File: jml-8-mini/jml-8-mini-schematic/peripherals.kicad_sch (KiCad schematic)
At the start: 10 parts, among them J2 Conn_01x09_Pin, J3 Conn_01x04_Pin, U4 Z80 CTC, U5 Z80 SIO

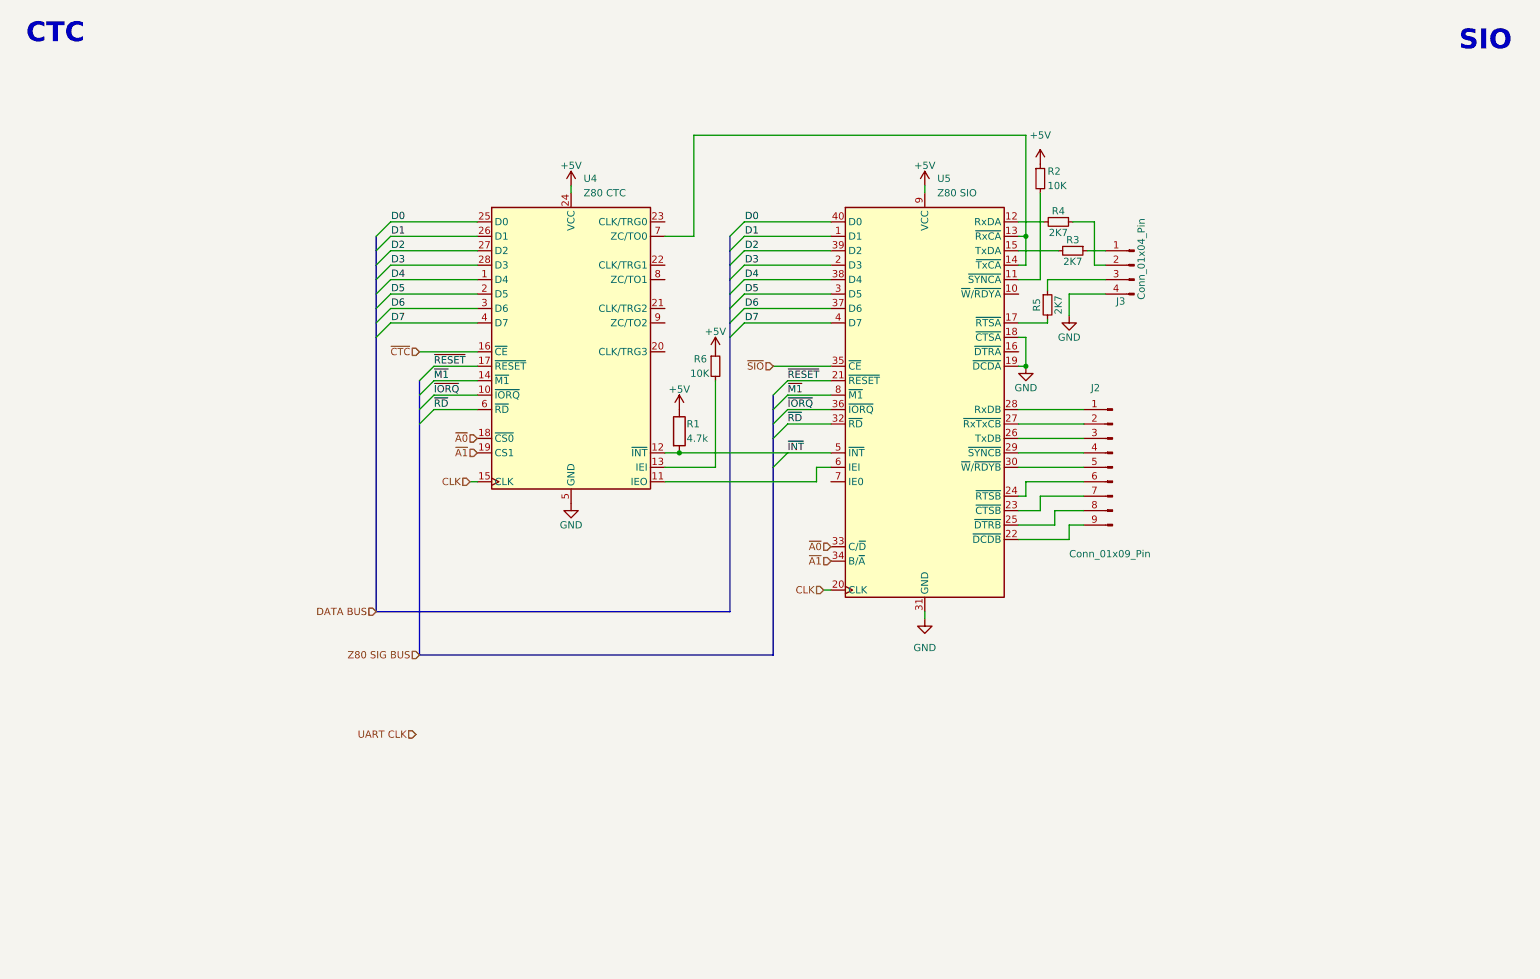
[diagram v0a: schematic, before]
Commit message: lots of changes to schematic, redone to make easier to read and add to
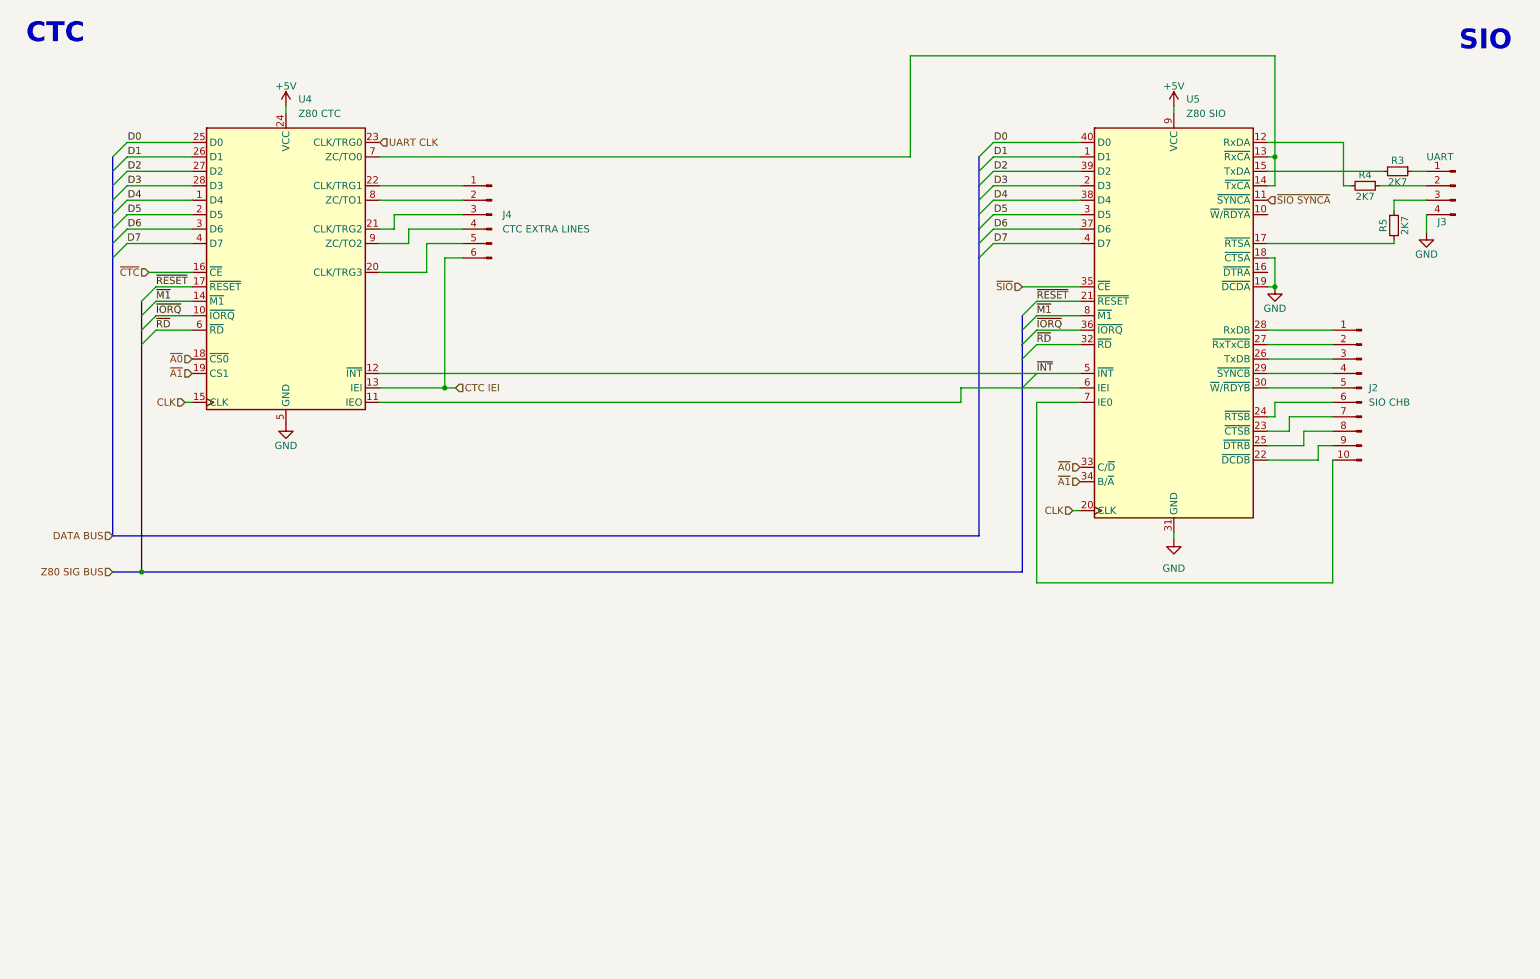
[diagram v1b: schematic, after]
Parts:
- removed J2: Conn_01x09_Pin, symbol Connector:Conn_01x09_Pin
- removed R1: 4.7k, symbol Device:R
- removed R2, R6: 10K, symbol Device:R_Small
- added J2: SIO CHB, symbol Connector:Conn_01x10_Pin
- added J4: CTC EXTRA LINES, symbol Connector:Conn_01x06_Pin
- J3: value Conn_01x04_Pin -> UART
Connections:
- net UART CLK: now also U4.23 (CLK/TRG0)
- net at U5.28 (RxDB): now also J2.1 (Pin_1)
- net at U5.27 (~{RxTxCB}): now also J2.2 (Pin_2)
- net at U5.26 (TxDB): now also J2.3 (Pin_3)
- net at U5.29 (~{SYNCB}): now also J2.4 (Pin_4)
- net at U5.30 (~{W}/~{RDYB}): now also J2.5 (Pin_5)
- net at U5.24 (~{RTSB}): now also J2.6 (Pin_6)
- net at U5.23 (~{CTSB}): now also J2.7 (Pin_7)
- net at U5.25 (~{DTRB}): now also J2.8 (Pin_8)
- net at U5.22 (~{DCDB}): now also J2.9 (Pin_9)
- net CTC IEI: now reaches U4.13 (IEI)
- net CTC IEI: now also J4.6 (Pin_6)
- net ~{SIO SYNCA}: now reaches U5.11 (~{SYNCA})
- net at U5.7 (IE0): now also J2.10 (Pin_10)
- net at U4.20 (CLK/TRG3): now also J4.5 (Pin_5)
- net at U4.21 (CLK/TRG2): now also J4.3 (Pin_3)
- net at U4.22 (CLK/TRG1): now also J4.1 (Pin_1)
- net at U4.8 (ZC/TO1): now also J4.2 (Pin_2)
- net at U4.9 (ZC/TO2): now also J4.4 (Pin_4)
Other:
- moved on the sheet: J3, R3, R5, U4, U5

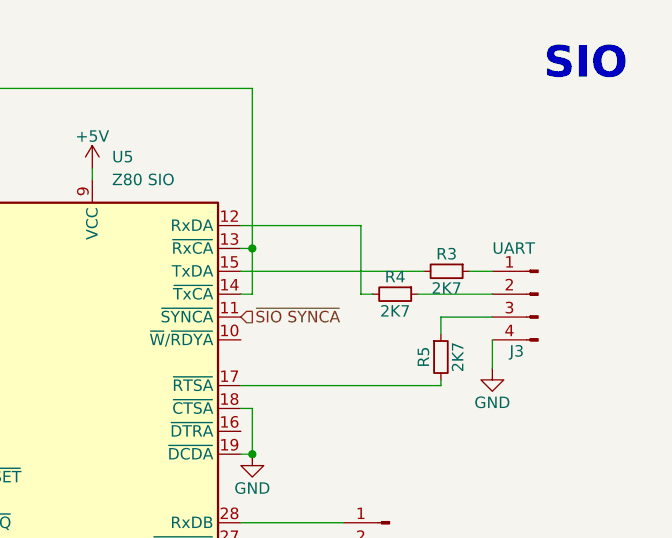
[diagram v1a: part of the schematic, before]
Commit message: updates to schematic, generally making formatting better
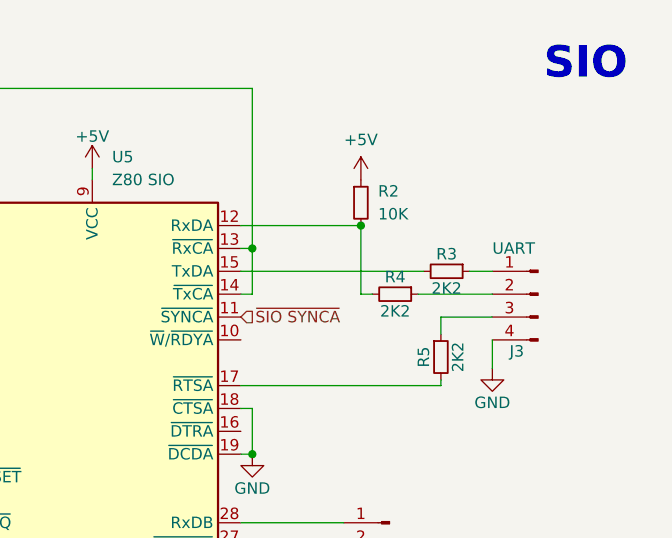
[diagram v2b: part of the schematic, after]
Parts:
- added R2: 10K, symbol Device:R_Small
- R3, R4, R5: value 2K7 -> 2K2
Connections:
- net +5V: now also R2.1
- net at R4.2, U5.12 (RxDA): now also R2.2
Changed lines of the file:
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@@
 (kicad_sch (version 20230121) (generator eeschema)
   (paper "A4")
+  (junction (at 248.285 38.735) (diameter 0) (color 0 0 0 0)
+  )
   (junction (at 236.22 41.275) (diameter 0) (color 0 0 0 0)
   )
@@
       (effects (font (size 1.27 1.27)))
     )
-    (property "Value" "2K7" (at 252.095 48.26 90)
+    (property "Value" "2K2" (at 252.095 48.26 90)
       (effects (font (size 1.27 1.27)))
     )
@@
     )
   )
+  (symbol (lib_id "Device:R_Small") (at 248.285 36.195 0) (unit 1)
+    (in_bom yes) (on_board yes) (dnp no) (fields_autoplaced)
+    (property "Reference" "R2" (at 250.19 34.925 0)
+      (effects (font (size 1.27 1.27)) (justify left))
+    )
+    (property "Value" "10K" (at 250.19 37.465 0)
+      (effects (font (size 1.27 1.27)) (justify left))
+    )
+    (property "Footprint" "" (at 248.285 36.195 0)
+      (effects (font (size 1.27 1.27)) hide)
+    )
+    (property "Datasheet" "~" (at 248.285 36.195 0)
+      (effects (font (size 1.27 1.27)) hide)
+    )
+    (pin "1")
+    (pin "2")
+    (instances
+      (project "jml-8-mini"
+        (path "/7f93abb4-2372-4a9e-a664-5edb67349db4/11c4238e-8051-4a00-8608-741a8b831ae1"
+          (reference "R2") (unit 1)
+        )
+      )
+    )
+  )
   (symbol (lib_id "Device:R_Small") (at 257.81 43.815 270) (unit 1)
     (in_bom yes) (on_board yes) (dnp no)
@@
       (effects (font (size 1.27 1.27)))
     )
-    (property "Value" "2K7" (at 257.81 45.72 90)
+    (property "Value" "2K2" (at 257.81 45.72 90)
       (effects (font (size 1.27 1.27)))
     )
@@
     )
   )
+  (symbol (lib_id "power:+5V") (at 248.285 33.655 0) (unit 1)
+    (in_bom yes) (on_board yes) (dnp no) (fields_autoplaced)
+    (property "Reference" "#PWR017" (at 248.285 37.465 0)
+      (effects (font (size 1.27 1.27)) hide)
+    )
+    (property "Value" "+5V" (at 248.285 29.21 0)
+      (effects (font (size 1.27 1.27)))
+    )
+    (property "Footprint" "" (at 248.285 33.655 0)
+      (effects (font (size 1.27 1.27)) hide)
+    )
+    (property "Datasheet" "" (at 248.285 33.655 0)
+      (effects (font (size 1.27 1.27)) hide)
+    )
+    (pin "1")
+    (instances
+      (project "jml-8-mini"
+        (path "/7f93abb4-2372-4a9e-a664-5edb67349db4/11c4238e-8051-4a00-8608-741a8b831ae1"
+          (reference "#PWR017") (unit 1)
+        )
+      )
+    )
+  )
   (symbol (lib_id "power:GND") (at 262.89 54.61 0) (unit 1)
     (in_bom yes) (on_board yes) (dnp no)
@@
       (effects (font (size 1.27 1.27)))
     )
-    (property "Value" "2K7" (at 259.08 53.34 90)
-      (effects (font (size 1.27 1.27)))
-    )
+    (property "Value" "2K2" (at 259.08 53.34 90)
+      (effects (font (size 1.27 1.27)))
+    )

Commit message: minor updates to schematic
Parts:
- removed R5: 2K2, symbol Device:R_Small
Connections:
- net GND: now also J3.3 (Pin_3)
- no-connect marks 0 -> 3
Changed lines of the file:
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@@
 (kicad_sch (version 20230121) (generator eeschema)
   (paper "A4")
+  (junction (at 262.89 51.435) (diameter 0) (color 0 0 0 0)
+  )
   (junction (at 248.285 38.735) (diameter 0) (color 0 0 0 0)
   )
@@
   (junction (at 236.22 64.135) (diameter 0) (color 0 0 0 0)
   )
+  (no_connect (at 234.95 61.595))
+  (no_connect (at 234.95 56.515))
+  (no_connect (at 234.95 51.435))
   (bus_entry (at 186.69 56.515) (size -2.54 2.54)
     (stroke (width 0) (type default))
@@
     (stroke (width 0) (type default))
   )
+  (wire (pts (xy 262.89 48.895) (xy 262.89 51.435))
+    (stroke (width 0) (type default))
+  )
   (wire (pts (xy 201.93 38.735) (xy 186.69 38.735))
     (stroke (width 0) (type default))
@@
     (stroke (width 0) (type default))
   )
-  (wire (pts (xy 257.175 48.895) (xy 262.89 48.895))
-    (stroke (width 0) (type default))
-  )
   (wire (pts (xy 236.22 64.135) (xy 234.95 64.135))
     (stroke (width 0) (type default))
@@
     (stroke (width 0) (type default))
   )
-  (wire (pts (xy 234.95 56.515) (xy 257.175 56.515))
-    (stroke (width 0) (type default))
-  )
   (wire (pts (xy 234.95 38.735) (xy 248.285 38.735))
     (stroke (width 0) (type default))
@@
     (stroke (width 0) (type default))
   )
-  (wire (pts (xy 257.175 56.515) (xy 257.175 55.88))
-    (stroke (width 0) (type default))
-  )
   (wire (pts (xy 81.28 51.435) (xy 93.345 51.435))
     (stroke (width 0) (type default))
@@
   )
   (bus (pts (xy 31.75 114.3) (xy 36.83 114.3))
-    (stroke (width 0) (type default))
-  )
-  (wire (pts (xy 257.175 50.8) (xy 257.175 48.895))
     (stroke (width 0) (type default))
   )
@@
         )
       )
-    )
-  )
-  (symbol (lib_id "Device:R_Small") (at 257.175 53.34 0) (unit 1)
-    (in_bom yes) (on_board yes) (dnp no)
-    (property "Reference" "R5" (at 255.27 53.34 90)
-      (effects (font (size 1.27 1.27)))
-    )
-    (property "Value" "2K2" (at 259.08 53.34 90)
-      (effects (font (size 1.27 1.27)))
-    )
-    (property "Footprint" "" (at 257.175 53.34 0)
-      (effects (font (size 1.27 1.27)) hide)
-    )
-    (property "Datasheet" "~" (at 257.175 53.34 0)
-      (effects (font (size 1.27 1.27)) hide)
-    )
-    (pin "1")
-    (pin "2")
-    (instances
-      (project "jml-8-mini"
-        (path "/7f93abb4-2372-4a9e-a664-5edb67349db4"
-          (reference "R5") (unit 1)
-        )
-        (path "/7f93abb4-2372-4a9e-a664-5edb67349db4/11c4238e-8051-4a00-8608-741a8b831ae1"
-          (reference "R4") (unit 1)
-        )
-      )
